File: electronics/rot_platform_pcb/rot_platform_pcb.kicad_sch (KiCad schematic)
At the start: 16 parts, among them J1 Motor_out, J2 Heating_conn, J3 Pump_conn, J4 Encoder_conn, J5 UART_Debug, J6 I2C_conn, J7 Endstop, J9 Power, Q1 IRLZ44N, Q2 IRLZ44N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

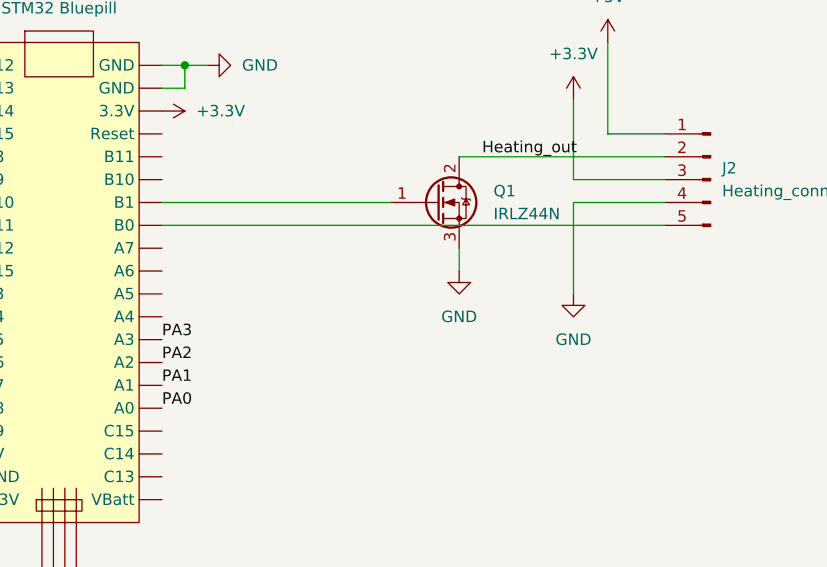
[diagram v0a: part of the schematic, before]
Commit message: update rotational stage PCB to V1.1
Fixed a few issues in V1.0
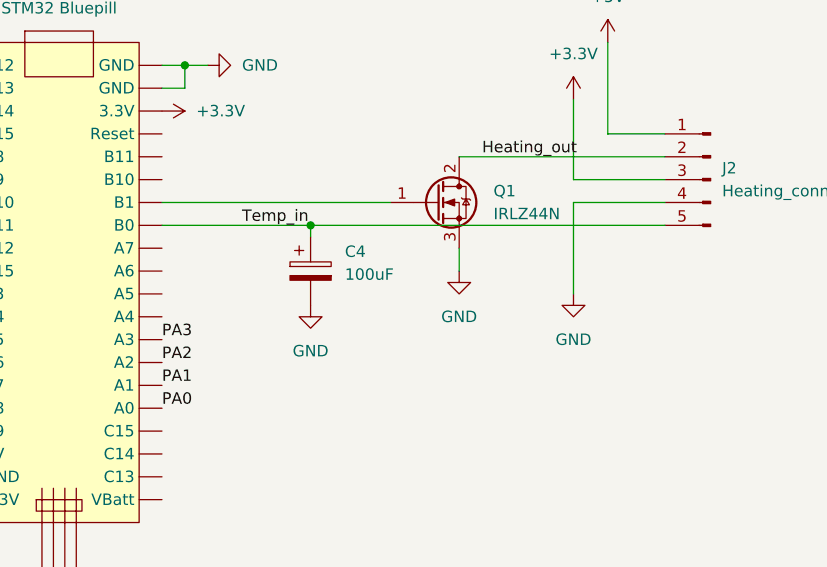
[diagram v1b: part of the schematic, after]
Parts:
- added C4: 100uF, Capacitor_THT:CP_Radial_D5.0mm_P2.50mm, symbol Device:C_Polarized
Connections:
- net GND: now also C4.2
- net Temp_in: now reaches J2.5 (Pin_5), U1.33 (B0)
- net Temp_in: now also C4.1
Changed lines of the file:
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@@
 		(color 0 0 0 0)
 	)
+	(junction
+		(at 195.58 90.17)
+		(diameter 0)
+		(color 0 0 0 0)
+	)
 	(wire
 		(pts
@@
 	(wire
 		(pts
+			(xy 195.58 91.44) (xy 195.58 90.17)
+		)
+		(stroke
+			(width 0)
+			(type default)
+		)
+	)
+	(wire
+		(pts
 			(xy 181.61 74.93) (xy 181.61 72.39)
 		)
@@
 	(wire
 		(pts
-			(xy 179.07 90.17) (xy 234.95 90.17)
+			(xy 179.07 90.17) (xy 195.58 90.17)
 		)
 		(stroke
@@
 		(pts
 			(xy 64.77 93.98) (xy 64.77 110.49)
+		)
+		(stroke
+			(width 0)
+			(type default)
+		)
+	)
+	(wire
+		(pts
+			(xy 195.58 90.17) (xy 234.95 90.17)
 		)
 		(stroke
@@
 	(label "PA3"
 		(at 179.07 102.87 0)
+		(effects
+			(font
+				(size 1.27 1.27)
+			)
+			(justify left bottom)
+		)
+	)
+	(label "Temp_in"
+		(at 187.96 90.17 0)
 		(effects
 			(font
@@
 	)
 	(symbol
+		(lib_id "Device:C_Polarized")
+		(at 195.58 95.25 0)
+		(unit 1)
+		(exclude_from_sim no)
+		(in_bom yes)
+		(on_board yes)
+		(dnp no)
+		(fields_autoplaced yes)
+		(property "Reference" "C4"
+			(at 199.39 93.0909 0)
+			(effects
+				(font
+					(size 1.27 1.27)
+				)
+				(justify left)
+			)
+		)
+		(property "Value" "100uF"
+			(at 199.39 95.6309 0)
+			(effects
+				(font
+					(size 1.27 1.27)
+				)
+				(justify left)
+			)
+		)
+		(property "Footprint" "Capacitor_THT:CP_Radial_D5.0mm_P2.50mm"
+			(at 196.5452 99.06 0)
+			(effects
+				(font
+					(size 1.27 1.27)
+				)
+				(hide yes)
+			)
+		)
+		(property "Datasheet" "~"
+			(at 195.58 95.25 0)
+			(effects
+				(font
+					(size 1.27 1.27)
+				)
+				(hide yes)
+			)
+		)
+		(property "Description" "Polarized capacitor"
+			(at 195.58 95.25 0)
+			(effects
+				(font
+					(size 1.27 1.27)
+				)
+				(hide yes)
+			)
+		)
+		(pin "1"
+		)
+		(pin "2"
+		)
+		(instances
+			(project "rot_platform_pcb"
+				(path "/945ae6c9-9f2c-4a61-a4d0-3d0e3f888461"
+					(reference "C4")
+					(unit 1)
+				)
+			)
+		)
+	)
+	(symbol
 		(lib_id "stm32_bluepill:stm32_bluepill")
 		(at 167.64 96.52 0)
@@
 					(unit 1)
 				)
+			)
+		)
+	)
+	(symbol
+		(lib_id "power:GND")
+		(at 195.58 99.06 0)
+		(unit 1)
+		(exclude_from_sim no)
+		(in_bom yes)
+		(on_board yes)
+		(dnp no)
+		(fields_autoplaced yes)
+		(property "Reference" "#PWR01"
+			(at 195.58 105.41 0)
+			(effects
+				(font
+					(size 1.27 1.27)
+				)
+				(hide yes)
+			)
+		)
+		(property "Value" "GND"
+			(at 195.58 104.14 0)
+			(effects
+				(font
+					(size 1.27 1.27)
+				)
+			)
+		)
+		(property "Footprint" ""
+			(at 195.58 99.06 0)
+			(effects
+				(font
+					(size 1.27 1.27)
+				)
+				(hide yes)
+			)
+		)
+		(property "Datasheet" ""
+			(at 195.58 99.06 0)
+			(effects
+				(font
+					(size 1.27 1.27)
+				)
+				(hide yes)
+			)
+		)
+		(property "Description" "Power symbol creates a global label with name \"GND\" , ground"
+			(at 195.58 99.06 0)
+			(effects
+				(font
+					(size 1.27 1.27)
+				)
+				(hide yes)
+			)
+		)
+		(pin "1"
+		)
+		(instances
+			(project "rot_platform_pcb"
+				(path "/945ae6c9-9f2c-4a61-a4d0-3d0e3f888461"
+					(reference "#PWR01")
+					(unit 1)
+				)
